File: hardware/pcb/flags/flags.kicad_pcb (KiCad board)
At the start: 2 copper layers, 62.2 x 21.6 mm, 42 parts, among them J1 Bus, J2 Control, J3 Sync, J4 Power, J5 Flags_Bus, J6 Ctrl_Out, U1 74HC02, U2 74HC08, U3 74HC157, U4 74HC173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

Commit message: Manual track touch-up
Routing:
- net ~OUT~: track 49.3 -> 50.5 mm
- net N_CTRL: track 5.33 -> 4.76 mm

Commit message: Adjust silk
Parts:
- D8: value USEC -> USC
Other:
- board text added: "~BOUT~ ~LOAD~ BIN USC"
- board text removed: "~OUT~ ~LOAD~ SEL USC"
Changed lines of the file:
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@@
   (general
     (thickness 1.6)
-    (drawings 44)
+    (drawings 46)
     (tracks 674)
     (zones 0)
@@
   (page A4)
   (layers
-    (0 F.Cu signal)
-    (31 B.Cu signal hide)
+    (0 F.Cu signal hide)
+    (31 B.Cu signal)
     (32 B.Adhes user hide)
     (33 F.Adhes user hide)
     (34 B.Paste user hide)
     (35 F.Paste user hide)
-    (36 B.SilkS user hide)
+    (36 B.SilkS user)
     (37 F.SilkS user hide)
     (38 B.Mask user hide)
@@
       (effects (font (size 1 1) (thickness 0.15)) (justify mirror))
     )
-    (fp_text value 10K (at 0 -1.65 90) (layer B.Fab)
+    (fp_text value 10K (at -2.785 -1.27 180) (layer B.SilkS)
       (effects (font (size 1 1) (thickness 0.15)) (justify mirror))
     )
@@
       (effects (font (size 1 1) (thickness 0.15)))
     )
-    (fp_text value Z (at -2.93 0 180) (layer F.SilkS)
+    (fp_text value Z (at -3.438 0 180) (layer F.SilkS)
       (effects (font (size 1 1) (thickness 0.15)))
     )
@@
       (effects (font (size 1 1) (thickness 0.15)))
     )
-    (fp_text value V (at -2.921 0 180) (layer F.SilkS)
+    (fp_text value V (at -3.429 0 180) (layer F.SilkS)
       (effects (font (size 1 1) (thickness 0.15)))
     )
@@
       (effects (font (size 1 1) (thickness 0.15)))
     )
-    (fp_text value N (at -2.93 0 180) (layer F.SilkS)
+    (fp_text value N (at -3.438 0 180) (layer F.SilkS)
       (effects (font (size 1 1) (thickness 0.15)))
     )
@@
       (effects (font (size 1 1) (thickness 0.15)))
     )
-    (fp_text value C (at -2.921 0 180) (layer F.SilkS)
+    (fp_text value C (at -3.429 0 180) (layer F.SilkS)
       (effects (font (size 1 1) (thickness 0.15)))
     )
@@
       (effects (font (size 1 1) (thickness 0.15)))
     )
-    (fp_text value USEC (at -4.032238 0.127) (layer F.SilkS)
+    (fp_text value USC (at -3.579857 0.127) (layer F.SilkS)
       (effects (font (size 1 1) (thickness 0.15)))
     )
@@
       (effects (font (size 1 1) (thickness 0.15)) (justify mirror))
     )
-    (fp_text value 330 (at 0 -1.65 270) (layer B.Fab)
+    (fp_text value 330 (at -2.531 -5.715) (layer B.SilkS)
       (effects (font (size 1 1) (thickness 0.15)) (justify mirror))
     )
@@
       (effects (font (size 1 1) (thickness 0.15)) (justify mirror))
     )
-    (fp_text value 330 (at 0 -1.65) (layer B.Fab)
+    (fp_text value 330 (at 0 -1.65) (layer B.SilkS)
       (effects (font (size 1 1) (thickness 0.15)) (justify mirror))
     )
@@
       (effects (font (size 1 1) (thickness 0.15)) (justify mirror))
     )
-    (fp_text value 10K (at 0 -1.65 270) (layer B.Fab)
+    (fp_text value 10K (at -2.413 -1.524) (layer B.SilkS)
       (effects (font (size 1 1) (thickness 0.15)) (justify mirror))
     )
@@
     )
   )
+  (gr_line (start 49.53 57.15) (end 49.784 57.15) (layer F.SilkS) (width 0.2))
+  (gr_line (start 49.53 54.61) (end 49.784 54.61) (layer F.SilkS) (width 0.2))
   (gr_line (start 49.53 57.15) (end 35.56 57.15) (layer F.SilkS) (width 0.2))
   (gr_line (start 35.56 54.61) (end 49.53 54.61) (layer F.SilkS) (width 0.2))
@@
     (effects (font (size 0.25 0.25) (thickness 0.0625)))
   )
-  (gr_text "~OUT~ ~LOAD~ SEL USC" (at 47.498 56.388) (layer F.SilkS)
+  (gr_text "~BOUT~ ~LOAD~ BIN USC" (at 47.498 56.388) (layer F.SilkS)
     (effects (font (size 0.25 0.25) (thickness 0.0625)))
   )
-  (gr_line (start 49.53 54.61) (end 49.53 57.15) (layer F.SilkS) (width 0.2))
+  (gr_line (start 49.784 54.61) (end 49.784 57.15) (layer F.SilkS) (width 0.2))
   (gr_line (start 53.34 57.15) (end 57.15 57.15) (layer F.SilkS) (width 0.2))
   (gr_line (start 53.34 54.61) (end 53.34 57.15) (layer F.SilkS) (width 0.2))
@@
     (effects (font (size 0.5 0.5) (thickness 0.1)))
   )
-  (gr_text "Velko 2020" (at 90.805 43.434) (layer F.SilkS)
+  (gr_text "Velko 2020" (at 74.676 55.88) (layer F.SilkS)
     (effects (font (size 0.75 0.75) (thickness 0.1875)))
   )
-  (gr_text "Flags v1.0" (at 90.17 41.148) (layer F.SilkS)
+  (gr_text "Flags v1.0" (at 90.17 42.418) (layer F.SilkS)
     (effects (font (size 1.25 1.25) (thickness 0.3)))
   )

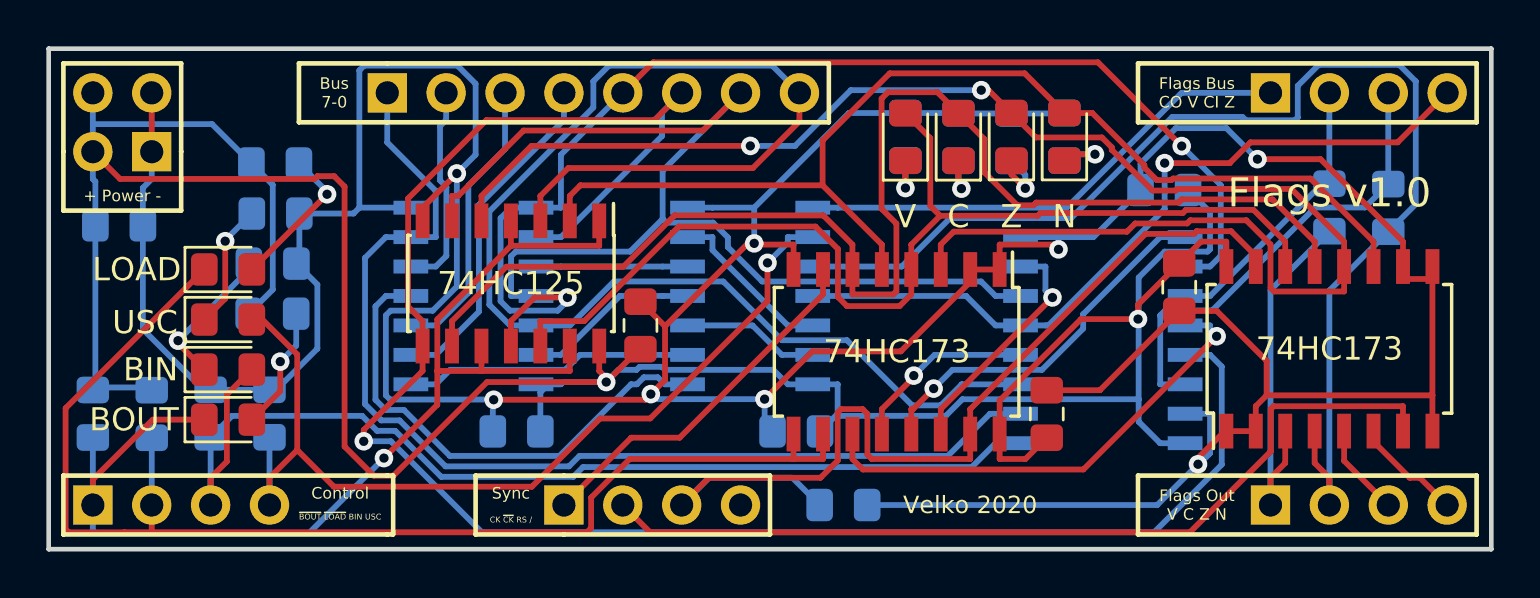
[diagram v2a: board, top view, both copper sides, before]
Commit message: Add copper pours
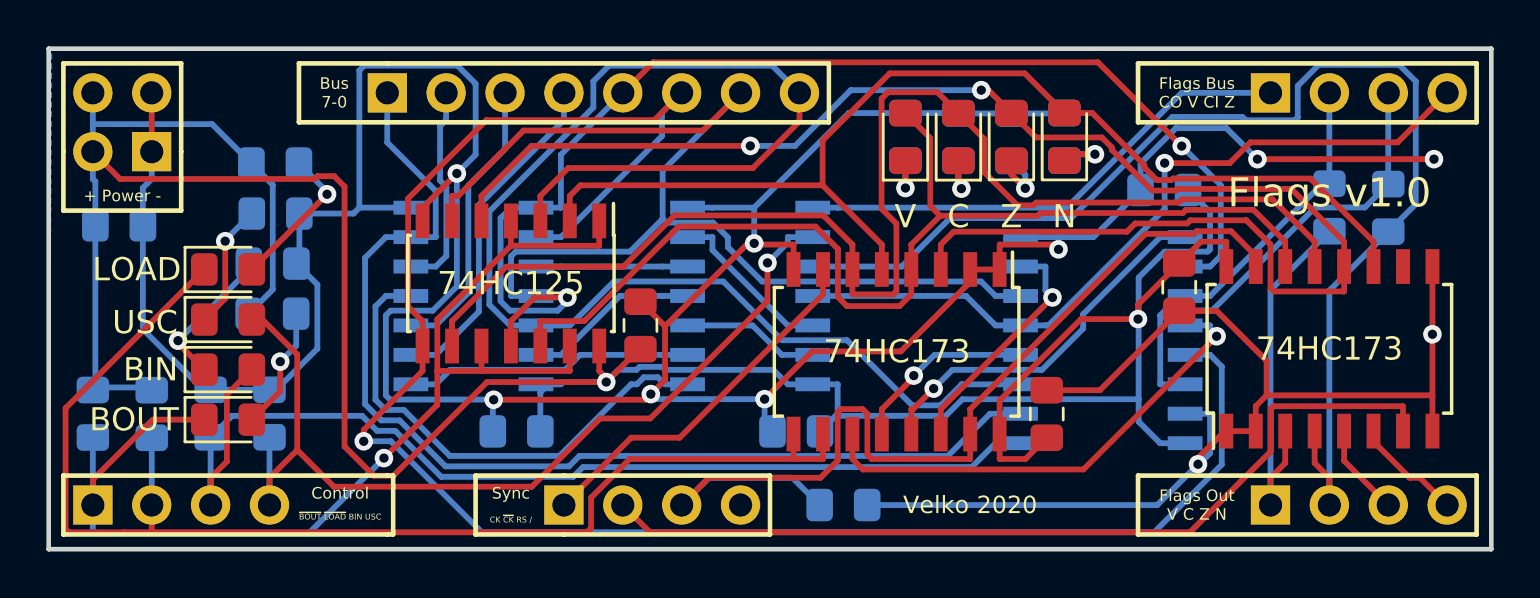
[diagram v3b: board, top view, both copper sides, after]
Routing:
- net GND: track 205.5 -> 203.0 mm, vias 8 -> 10
- added copper zone on B.Cu, net GND
- added copper zone on F.Cu, net VCC
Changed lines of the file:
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@@
     (thickness 1.6)
     (drawings 46)
-    (tracks 674)
+    (tracks 676)
     (zones 0)
     (modules 42)
@@
   (page A4)
   (layers
-    (0 F.Cu signal hide)
-    (31 B.Cu signal)
+    (0 F.Cu signal)
+    (31 B.Cu signal hide)
     (32 B.Adhes user hide)
     (33 F.Adhes user hide)
@@
     (last_trace_width 0.25)
     (trace_clearance 0.2)
-    (zone_clearance 0.508)
+    (zone_clearance 0.254)
     (zone_45_only no)
     (trace_min 0.2)
@@
   (segment (start 86.995 52.693) (end 86.995 52.1553) (width 0.25) (layer F.Cu) (net 2))
   (segment (start 94.615 51.1491) (end 94.615 52.693) (width 0.25) (layer F.Cu) (net 2))
-  (segment (start 94.615 46.1306) (end 94.615 51.1491) (width 0.25) (layer F.Cu) (net 2))
+  (segment (start 94.615 46.1306) (end 94.615 48.514) (width 0.25) (layer F.Cu) (net 2))
   (segment (start 65.8066 51.3128) (end 61.1166 51.3128) (width 0.25) (layer B.Cu) (net 2))
   (segment (start 61.1166 51.3128) (end 60.8994 51.0956) (width 0.25) (layer B.Cu) (net 2))
@@
   (segment (start 39.37 41.8153) (end 38.989 42.1963) (width 0.25) (layer B.Cu) (net 2))
   (segment (start 38.989 42.1963) (end 38.989 43.815) (width 0.25) (layer B.Cu) (net 2))
-  (segment (start 93.345 45.593) (end 93.345 44.5177) (width 0.25) (layer F.Cu) (net 2))
-  (segment (start 93.345 44.5177) (end 89.7883 40.961) (width 0.25) (layer F.Cu) (net 2))
   (segment (start 89.7883 40.961) (end 87.066 40.961) (width 0.25) (layer F.Cu) (net 2))
   (segment (start 93.345 45.8618) (end 93.345 45.593) (width 0.25) (layer F.Cu) (net 2))
   (segment (start 41.91 50.909) (end 44.45 50.909) (width 0.25) (layer B.Cu) (net 2))
   (segment (start 39.37 40.64) (end 39.37 39.4647) (width 0.25) (layer F.Cu) (net 2))
-  (segment (start 93.345 46.1306) (end 94.615 46.1306) (width 0.25) (layer F.Cu) (net 2))
   (segment (start 94.615 45.593) (end 94.615 46.1306) (width 0.25) (layer F.Cu) (net 2))
   (segment (start 93.345 45.8618) (end 93.345 46.1306) (width 0.25) (layer F.Cu) (net 2))
@@
   (segment (start 74.676 45.72) (end 75.946 45.72) (width 0.25) (layer F.Cu) (net 2))
   (segment (start 86.995 52.693) (end 85.725 52.693) (width 0.25) (layer F.Cu) (net 2))
+  (segment (start 89.7883 40.961) (end 94.682 40.961) (width 0.25) (layer F.Cu) (net 2))
+  (segment (start 94.682 40.961) (end 94.682 40.961) (width 0.25) (layer F.Cu) (net 2))
+  (via (at 94.682 40.961) (size 0.8) (drill 0.4) (layers F.Cu B.Cu) (net 2))
+  (segment (start 94.615 48.514) (end 94.615 51.1491) (width 0.25) (layer F.Cu) (net 2))
+  (via (at 94.615 48.514) (size 0.8) (drill 0.4) (layers F.Cu B.Cu) (net 2))
   (segment (start 85.725 45.593) (end 85.725 44.5177) (width 0.25) (layer F.Cu) (net 3))
   (segment (start 85.725 44.5177) (end 84.6323 44.5177) (width 0.25) (layer F.Cu) (net 3))
@@
   (segment (start 70.866 52.82) (end 70.866 51.7447) (width 0.25) (layer F.Cu) (net 48))
   (via (at 72.242 50.2971) (size 0.8) (layers F.Cu B.Cu) (net 48))
+  (zone (net 2) (net_name GND) (layer B.Cu) (hatch edge 0.508)
+    (connect_pads (clearance 0.254))
+    (min_thickness 0.254)
+    (fill yes (arc_segments 16) (thermal_gap 0.508) (thermal_bridge_width 0.508))
+    (polygon
+      (pts
+        (xy 35.052 36.195) (xy 97.155 36.195) (xy 97.155 57.785) (xy 34.925 57.785)
+      )
+    )
+  )
+  (zone (net 3) (net_name VCC) (layer F.Cu) (hatch edge 0.508)
+    (connect_pads (clearance 0.254))
+    (min_thickness 0.254)
+    (fill yes (arc_segments 16) (thermal_gap 0.508) (thermal_bridge_width 0.508))
+    (polygon
+      (pts
+        (xy 34.925 36.195) (xy 97.155 36.195) (xy 97.155 57.785) (xy 34.925 57.785)
+      )
+    )
+  )
 )

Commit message: Update cap annotation - μF
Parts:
- C7: value 10uF -> 10μF
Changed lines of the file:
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@@
       (effects (font (size 1 1) (thickness 0.15)) (justify mirror))
     )
-    (fp_text value 10uF (at 0 1.905) (layer B.SilkS)
+    (fp_text value 10μF (at 0 1.905) (layer B.SilkS)
       (effects (font (size 1 1) (thickness 0.15)) (justify mirror))
     )
